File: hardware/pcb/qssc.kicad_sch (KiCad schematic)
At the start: 84 parts, among them J1 FT232RL, J10 USB-C, J2 5V Barrel, J3 SMA, J4 Emitter drv, J5 Detector FE, J6 DET_BIAS, J7 RESET, J8 MW_GATE, J9 JTAG, U1 XC7A35T-1CPG236C, U3 ADF4351BCPZ, U5 HMC441LP3E, U7 ADA4530-1, U8 W25Q128JVSIQ, Y1 100MHz TCXO

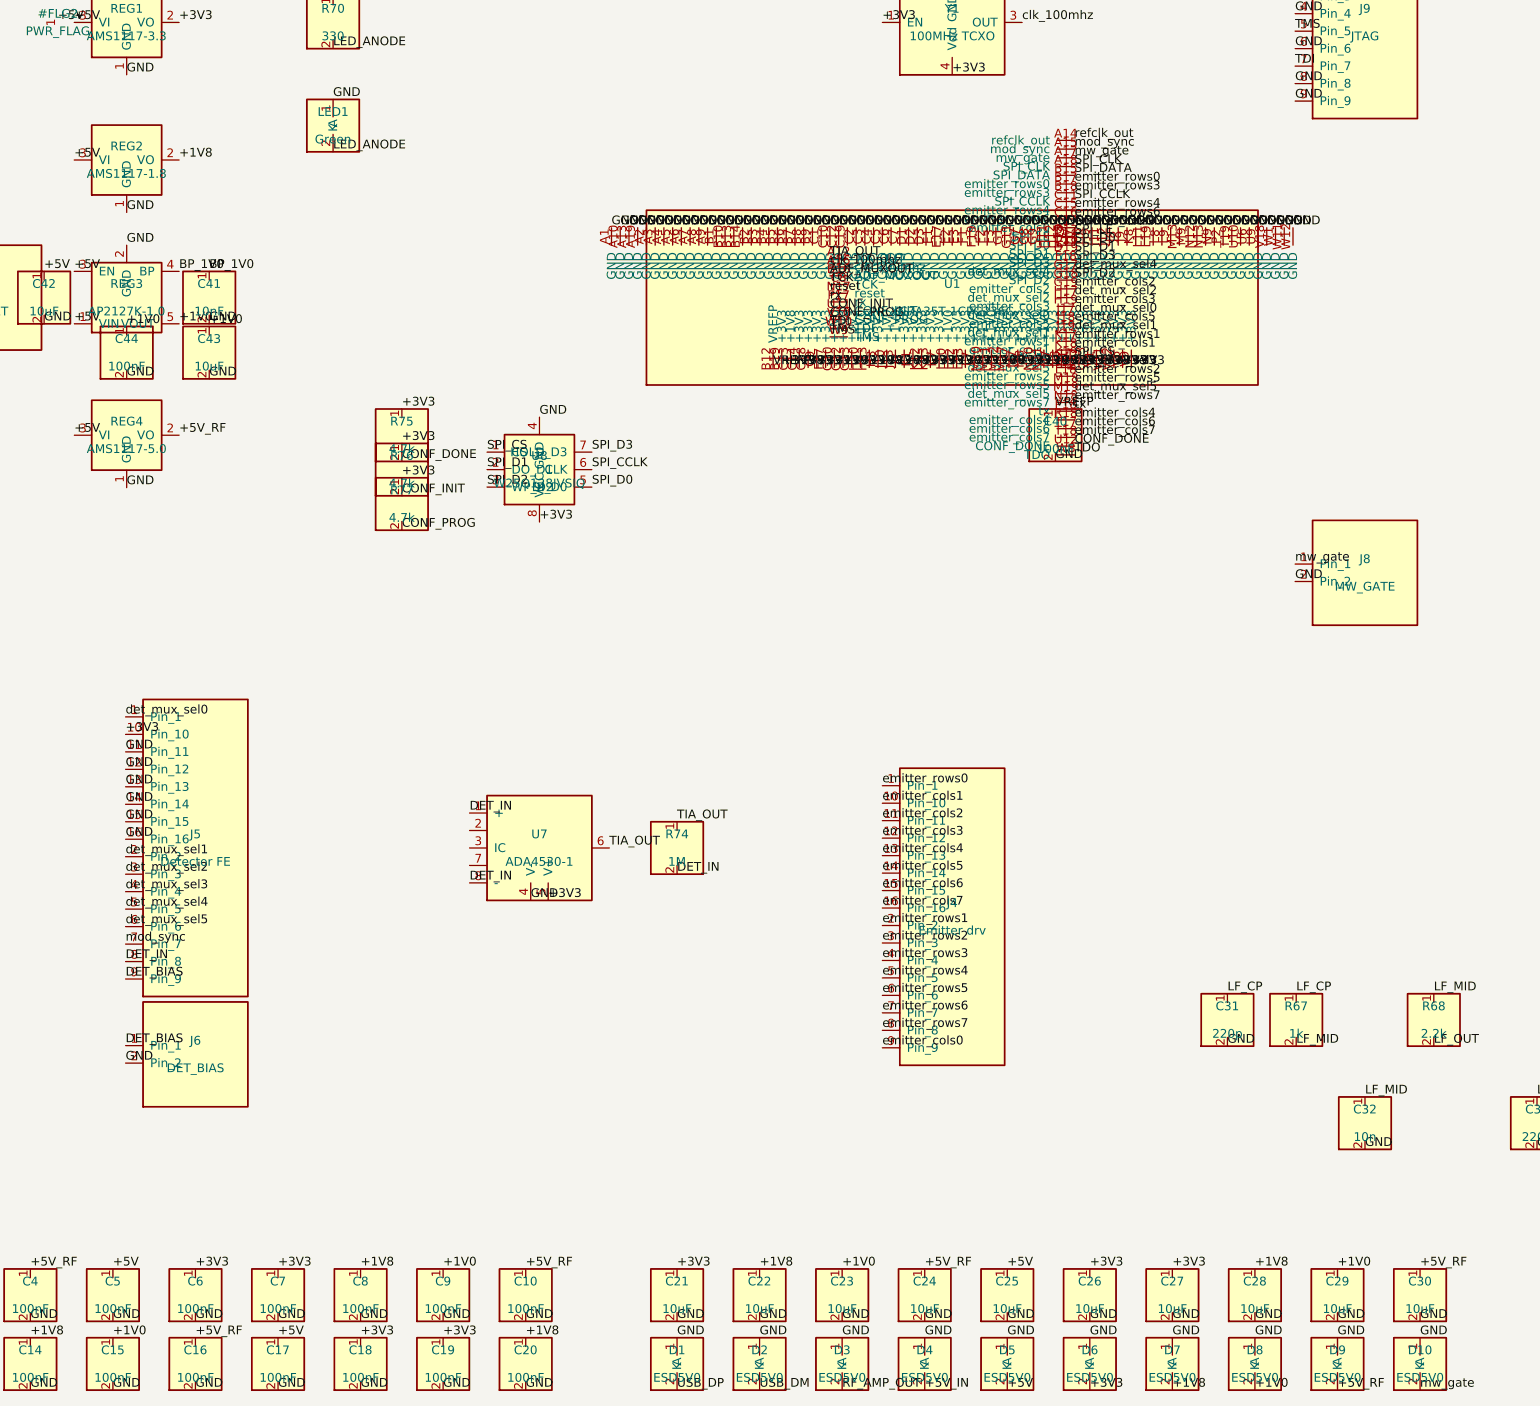
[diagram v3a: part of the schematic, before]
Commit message: PCB: conectador board-to-board J11 (Samtec LSHM-130) + corrije cortocircuito esquemático del FPGA
* Añade J11 (Samtec LSHM-130 2x30 0.5 mm) como "socket" del módulo hija con
  front-end analógico (MUX 64:1 + TIA + driver CQD + Peltier). 60 pines netted:
  filas/cols del emisor (8+8), det_mux_sel[5:0], mod_sync, TIA_OUT, TIA_REF,
  DET_BIAS, THRM, +3V3/+5V/+7V_EMIT, y GND en todos los pines pares (retorno
  por señal). Sustituye el bloque analógico J4/J5/J6/R74/U7 placeholder.
* REG3 pasa a AP2127K-1.0 (Diodes Inc SOT-23-5): LDO real de 1.0 V para
  VCCINT — AMS1117 no tiene opción 1.0 V (mín 1.5 V). Símbolo autorizado por
  datasheet (1=VIN 2=GND 3=EN 4=BP 5=VOUT) + descargas C41-C44 + PWR_FLAG VREFP.
* Corrige cortocircuito esquemático en fpga_pin_list: las columnas de pines
  señal (x=±17.78) coincidían en la esquina con la fila GND inferior (y=10.16),
  dejando dos etiquetas (señal + GND) en el mismo punto → ERC multiple_net_names
  fundía la señal a GND (le pasó a emitter_cols0/C17). Movido a x=±50.8 (fuera
  del alcance de la fila, máx 49.53), on-grid, sin colisión.
* Movido J11 a (24,64): en (30,45) solapaba courtyards de C43/C44/REG4 y
  cortocircuitaba pads de descarga con pads de emitter_cols (DRC shorting_items).

Verificación: ERC 0 errores; DRC 0 errores/0 warnings/0 desconectados;
pytest 122 passed 2 skipped; XDC ports ok; emitter_cols0 = net 56 ≠ GND net 17.

Co-Authored-By: Claude <noreply@anthropic.com>
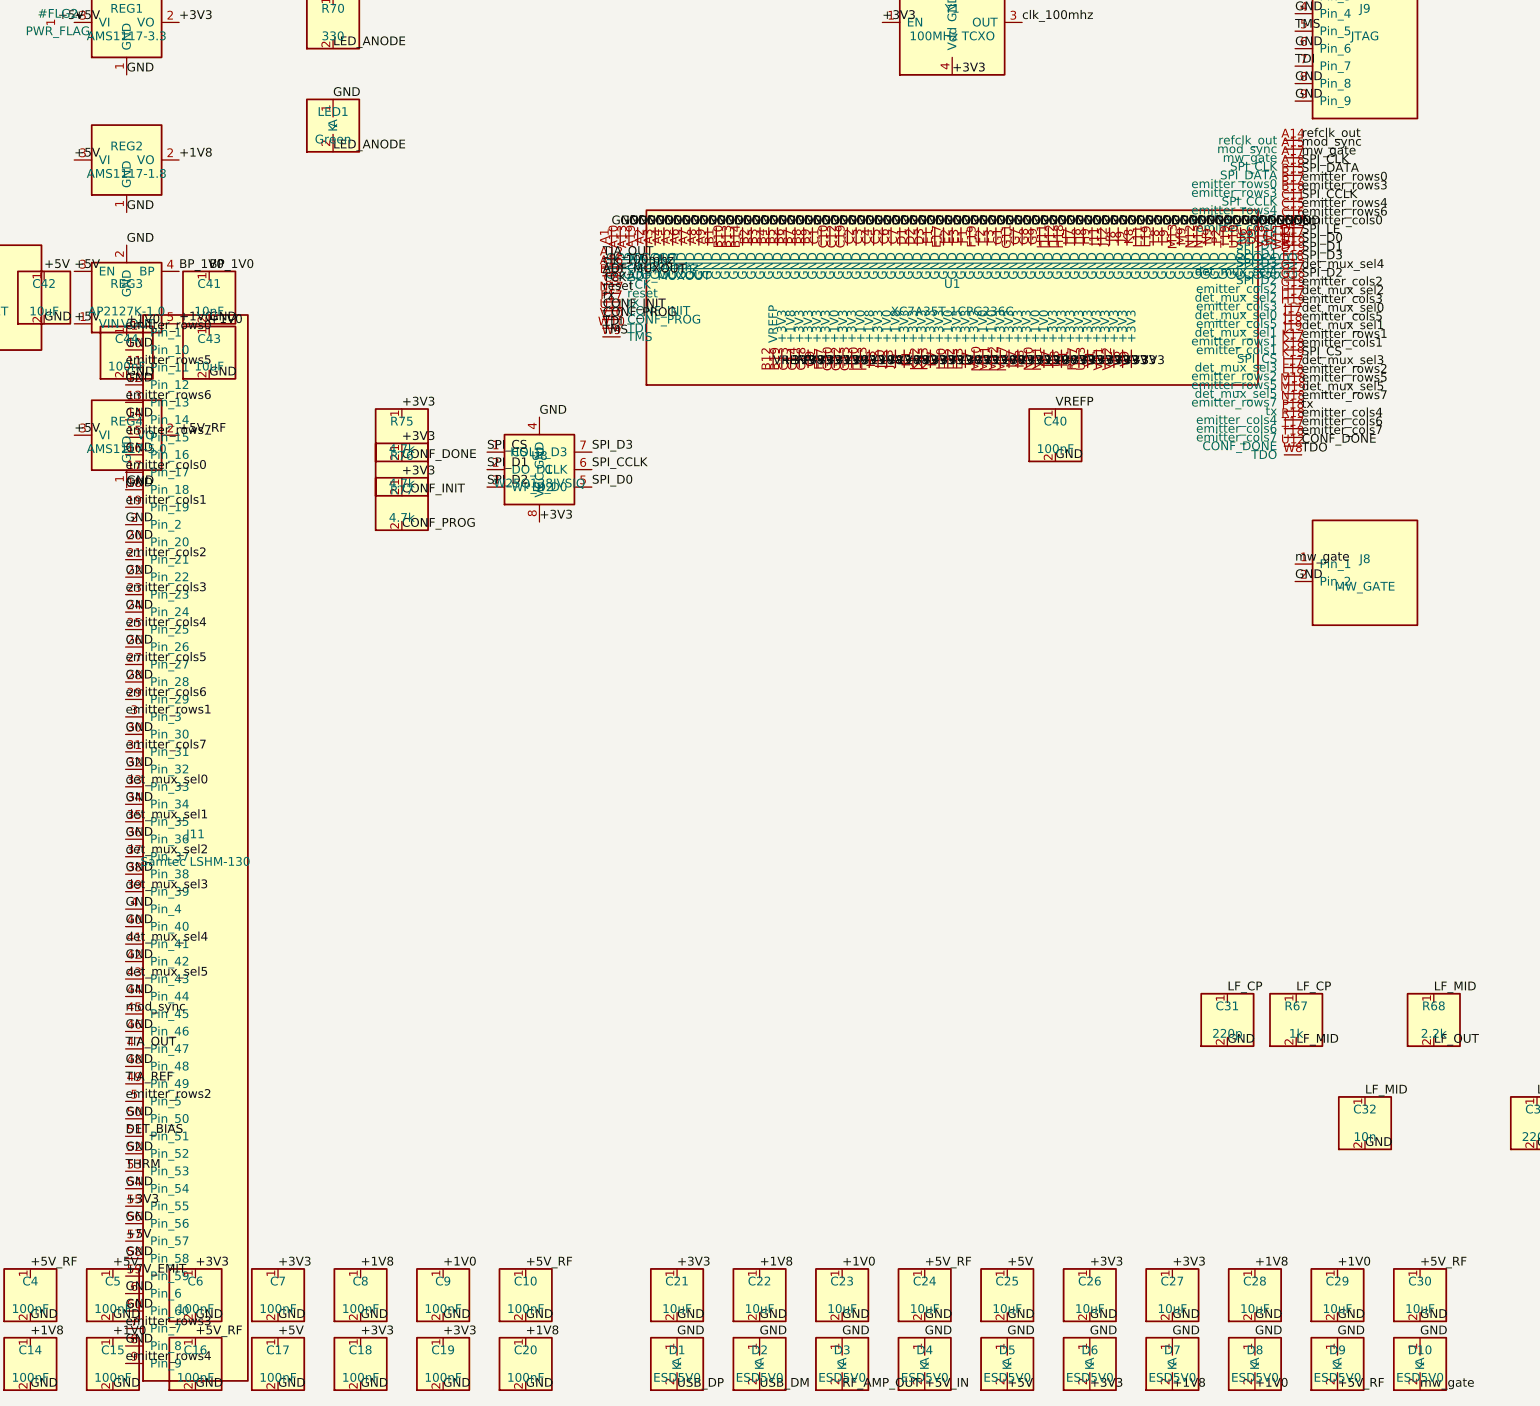
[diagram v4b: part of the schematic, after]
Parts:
- removed J4: Emitter drv, Connector_PinHeader_2.54mm:PinHeader_2x08_P2.54mm_Vertical, symbol qssc:Conn_02x08
- removed J5: Detector FE, Connector_PinHeader_2.54mm:PinHeader_2x08_P2.54mm_Vertical, symbol qssc:Conn_02x08
- removed J6: DET_BIAS, Connector_PinHeader_2.54mm:PinHeader_1x02_P2.54mm_Vertical, symbol qssc:Conn_01x02
- removed R74: 1M, Resistor_SMD:R_0603_1608Metric, symbol qssc:R
- removed U7: ADA4530-1, Package_SO:SOIC-8_3.9x4.9mm_P1.27mm, symbol qssc:ADA4530-1
- added J11: Samtec LSHM-130, Connector_Samtec:Samtec_LSHM-130-xx.x-x-DV-N_2x30_P0.50mm_Vertical, symbol qssc:Conn_02x30_Odd_Even
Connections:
- net +3V3: now also J11.55 (Pin_55)
- net +5V: now also J11.57 (Pin_57)
- net DET_BIAS: now also J11.51 (Pin_51)
- net GND: now also J11.10 (Pin_10), J11.12 (Pin_12), J11.14 (Pin_14), J11.16 (Pin_16), J11.18 (Pin_18), J11.2 (Pin_2), J11.20 (Pin_20), J11.22 (Pin_22), J11.24 (Pin_24), J11.26 (Pin_26), J11.28 (Pin_28), J11.30 (Pin_30), J11.32 (Pin_32), J11.34 (Pin_34), J11.36 (Pin_36), J11.38 (Pin_38), J11.4 (Pin_4), J11.40 (Pin_40), J11.42 (Pin_42), J11.44 (Pin_44), J11.46 (Pin_46), J11.48 (Pin_48), J11.50 (Pin_50), J11.52 (Pin_52), J11.54 (Pin_54), J11.56 (Pin_56), J11.58 (Pin_58), J11.6 (Pin_6), J11.60 (Pin_60), J11.8 (Pin_8); no longer U1.C17 (emitter_cols0)
- net TIA_OUT: now also J11.47 (Pin_47)
- net det_mux_sel0: now also J11.33 (Pin_33)
- net det_mux_sel1: now also J11.35 (Pin_35)
- net det_mux_sel2: now also J11.37 (Pin_37)
- net det_mux_sel3: now also J11.39 (Pin_39)
- net det_mux_sel4: now also J11.41 (Pin_41)
- net det_mux_sel5: now also J11.43 (Pin_43)
- net emitter_cols1: now also J11.19 (Pin_19)
- net emitter_cols2: now also J11.21 (Pin_21)
- net emitter_cols3: now also J11.23 (Pin_23)
- net emitter_cols4: now also J11.25 (Pin_25)
- net emitter_cols5: now also J11.27 (Pin_27)
- net emitter_cols6: now also J11.29 (Pin_29)
- net emitter_cols7: now also J11.31 (Pin_31)
- net emitter_rows0: now also J11.1 (Pin_1)
- net emitter_rows1: now also J11.3 (Pin_3)
- net emitter_rows2: now also J11.5 (Pin_5)
- net emitter_rows3: now also J11.7 (Pin_7)
- net emitter_rows4: now also J11.9 (Pin_9)
- net emitter_rows5: now also J11.11 (Pin_11)
- net emitter_rows6: now also J11.13 (Pin_13)
- net emitter_rows7: now also J11.15 (Pin_15)
- net mod_sync: now also J11.45 (Pin_45)
- new net +7V_EMIT: J11.59 (Pin_59)
- new net THRM: J11.53 (Pin_53)
- new net TIA_REF: J11.49 (Pin_49)
- new net emitter_cols0: J11.17 (Pin_17), U1.C17 (emitter_cols0)

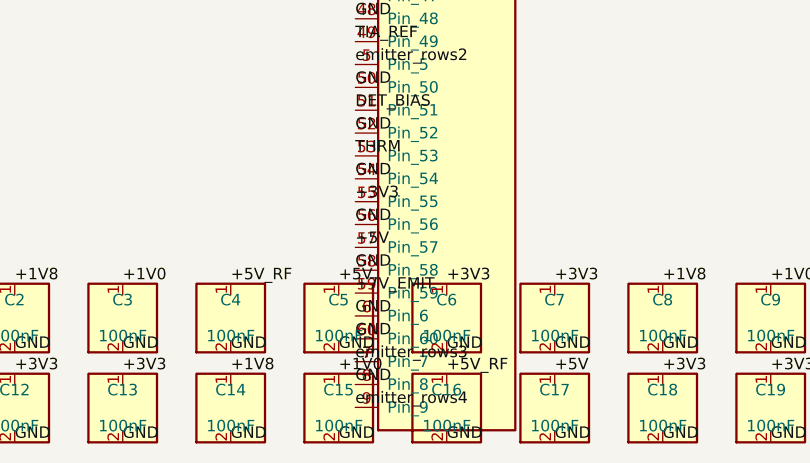
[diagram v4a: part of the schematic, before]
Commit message: chip module: place discrete MOSFET emitter crossbar (+5V), eliminate +7V_EMIT
Emitter driver for the 8x8 CQD matrix is now placed on the swappable chip
module as the simplest-functional topology (29 parts, no boost / no DAC /
no TLC5955): 2x 74HCT240 inverting level-shifters (3.3V FPGA -> 0/5V gate
drive, HCT TTL thresholds) + 8x AO3401A P-MOS high-side row switches +
8x AO3400A N-MOS low-side column sinks + 8x 220R set resistors + 3
decoupling. One pixel at a time, ~9mA at 2.2V headroom, matching
emitter_array.v (rows active-HIGH / cols active-LOW one-hot, idle all OFF).

Chip ER/EC pads rewired through the driver (ER{i}->emitter_anode{i},
EC{i}->emitter_cathode{i}); J1 still carries emitter_rows/cols -> 74HCT240
inputs. +7V_EMIT rail fully deleted on both boards: J1/J11 pin 59 -> GND
(extra pulsed-current return; connectors stay pin-for-pin mated), module
POWER_PINS/POWER_NETS/C6/#FLG3 removed. TIA is photovoltaic / zero-bias
(no MCP4921 DAC; DET_BIAS is a reserved spare). Module widened 70->85x50mm.

Verified headless: module ERC 0 errors / 53 warnings; module DRC 0
violations; main board ERC 0 errors / 139 warnings, DRC 0 violations.
pytest 122 passed / 2 skipped; ruff CI-gate clean. HARDWARE_DESIGN.md
\S1B/\S2/\S3/\S7/\S8/\S11/\S12/\S13/\S15A updated. RTL/XDC/sim/synth
untouched; new ~24 nets not yet routed (deferred GUI batch).

Co-Authored-By: Claude <noreply@anthropic.com>
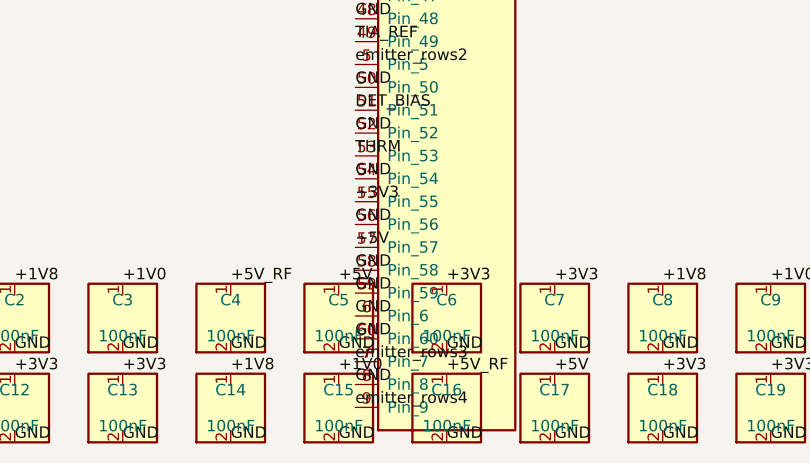
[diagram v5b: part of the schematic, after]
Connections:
- net +7V_EMIT is gone; now on net GND: J11.59 (Pin_59)
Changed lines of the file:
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@@
 		)
 	)
-	(label "+7V_EMIT"
+	(label "GND"
 		(at 79.84 212.23 0)
 		(fields_autoplaced yes)
